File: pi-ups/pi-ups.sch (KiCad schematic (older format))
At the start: 35 parts, among them J1 , Q1 IRLML2244, Q2 IRLML2244, Q3 IRLML2244, Q4 IRLML2244, U1 BMS_1S, U2 DC-DC, U3 BMS_1S, U4 FTDI232, U5 Arduino_Pro_Mini

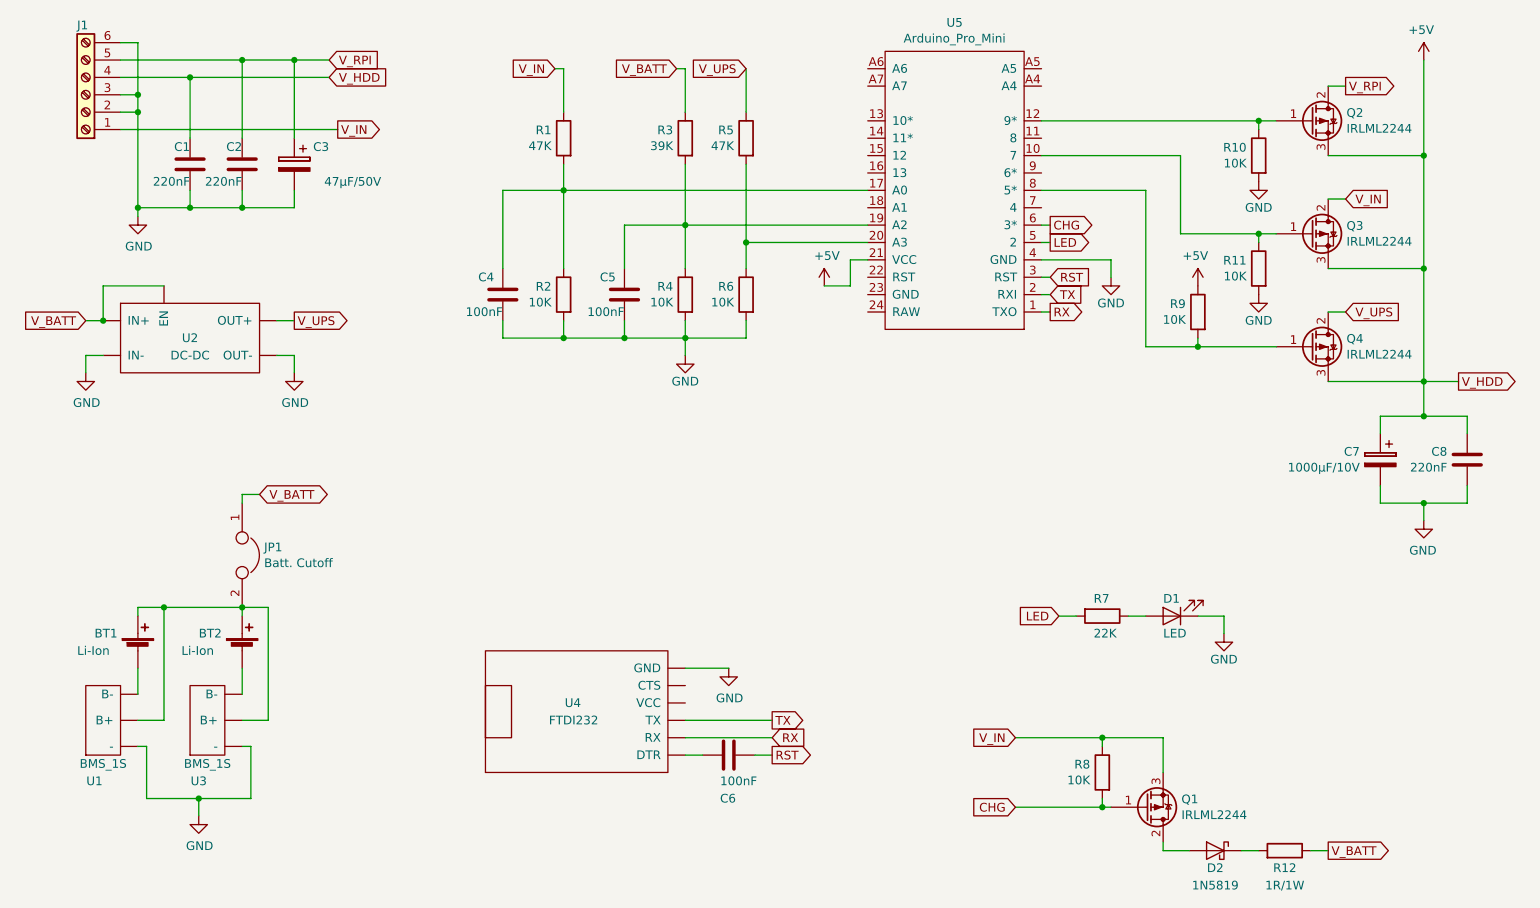
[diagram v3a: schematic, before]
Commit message: Update pi-ups.sch
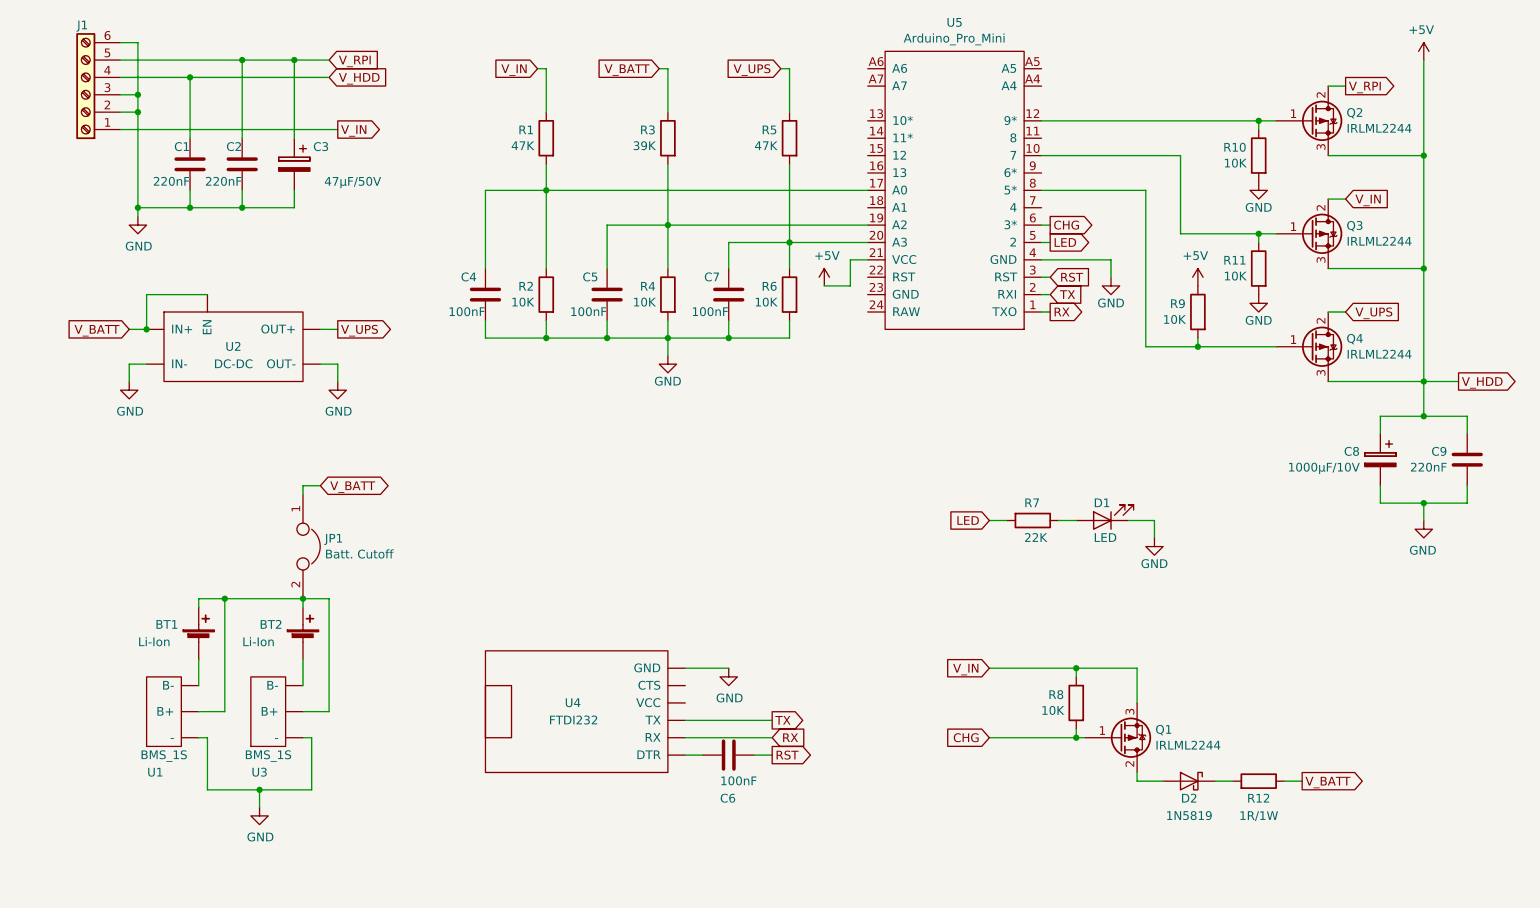
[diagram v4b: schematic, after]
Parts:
- added C7: 100nF, symbol Device:C
- renumbered C7 to C8, C8 to C9
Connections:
- net GND: now also C7.2
- net at R5.2, R6.1, U5.20 (A3): now also C7.1
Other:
- moved on the sheet: BT1, BT2, C4, C5, D1, D2, JP1, Q1, R1, R12, R2, R3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

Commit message: Update pi-ups.sch
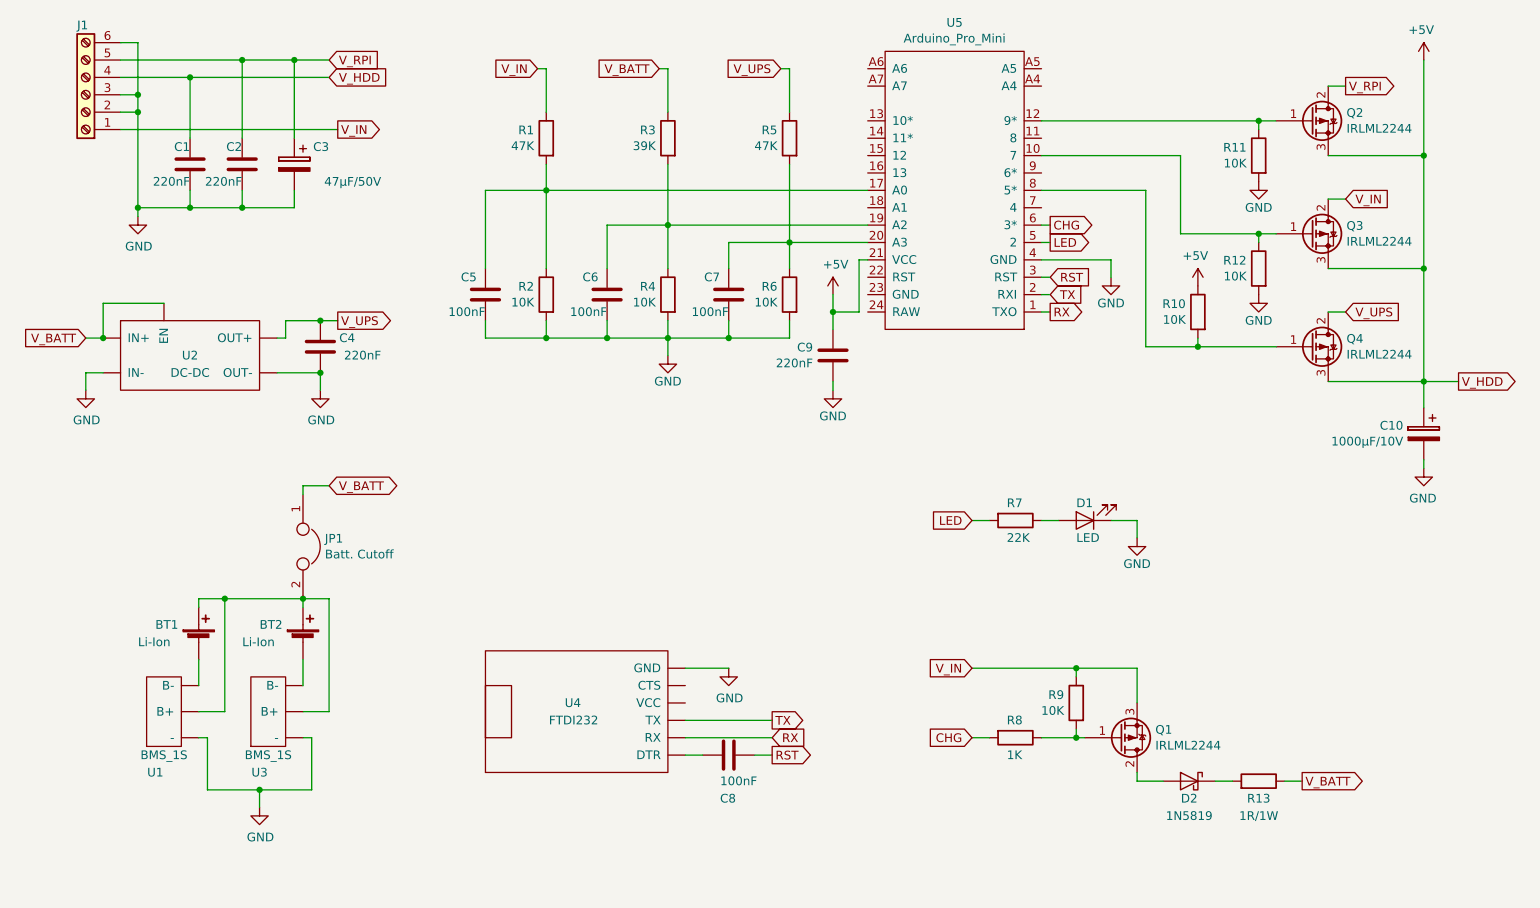
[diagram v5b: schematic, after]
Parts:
- added C4: 220nF, symbol Device:C
- added R8: 1K, symbol Device:R
- renumbered C8 to C10, C4 to C5, C5 to C6, C6 to C8, R9 to R10, R10 to R11, R11 to R12, R12 to R13, R8 to R9
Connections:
- net CHG: now also R8.2; no longer Q1.1 (G), R9.2
- net GND: now also C4.2
- net V_UPS: now also C4.1
- new net: Q1.1 (G), R8.1, R9.2
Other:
- moved on the sheet: C10, C9, D1, R7, U2
